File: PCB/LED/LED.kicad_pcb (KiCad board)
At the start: 2 copper layers, 70 x 70 mm, 23 parts, among them J1 Conn_01x03, J2 Conn_01x03, J5 USB-C-Socket-H, U6 ESP32-S3-MINI-1, U7 MD8942

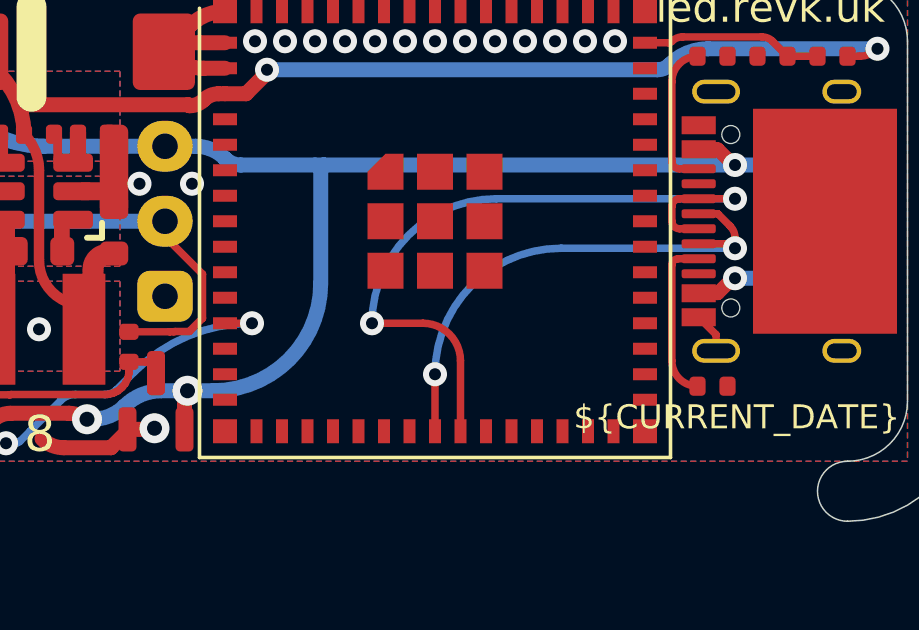
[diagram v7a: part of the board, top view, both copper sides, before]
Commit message: USB pads for in panel flashing
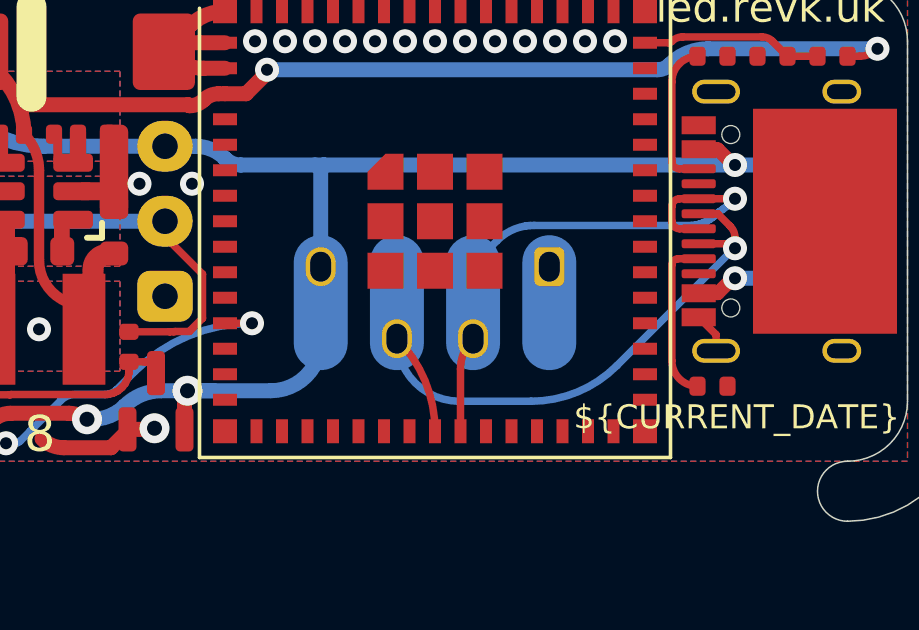
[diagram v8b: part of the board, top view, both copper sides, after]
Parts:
- added J3: USB-PROG, RevK:USB-PROG2, B.Cu at (104.8, 104.7)
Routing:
- net D+: track 24.0 -> 16.4 mm, vias 2 -> 1
- net D-: track 17.4 -> 21.0 mm, vias 2 -> 1
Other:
- board text removed: "A"
- board text removed: "B"
